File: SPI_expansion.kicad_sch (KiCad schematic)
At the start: 5 parts, among them J1 Conn_02x05_Odd_Even

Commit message: Latest updates
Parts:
- renumbered J1 to J9, R1 to R10, R2 to R11, R3 to R12, R4 to R13
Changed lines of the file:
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@@
 		(dnp no)
 		(fields_autoplaced yes)
-		(property "Reference" "#PWR06"
+		(property "Reference" "#PWR033"
 			(at 172.72 29.21 0)
 			(effects
@@
 			(project ""
 				(path "/38f33acd-ac87-4918-9c1f-d78977d10c9f/f251d033-7c4f-4f74-b0e8-105a8a585980"
-					(reference "#PWR06")
+					(reference "#PWR033")
 					(unit 1)
 				)
@@
 		(dnp no)
 		(fields_autoplaced yes)
-		(property "Reference" "R1"
+		(property "Reference" "R10"
 			(at 168.91 24.13 90)
 			(effects
@@
 			(project ""
 				(path "/38f33acd-ac87-4918-9c1f-d78977d10c9f/f251d033-7c4f-4f74-b0e8-105a8a585980"
-					(reference "R1")
+					(reference "R10")
 					(unit 1)
 				)
@@
 		(dnp no)
 		(fields_autoplaced yes)
-		(property "Reference" "R2"
+		(property "Reference" "R11"
 			(at 168.91 26.67 90)
 			(effects
@@
 			(project "OhWare"
 				(path "/38f33acd-ac87-4918-9c1f-d78977d10c9f/f251d033-7c4f-4f74-b0e8-105a8a585980"
-					(reference "R2")
+					(reference "R11")
 					(unit 1)
 				)
@@
 		(dnp no)
 		(fields_autoplaced yes)
-		(property "Reference" "J1"
+		(property "Reference" "J9"
 			(at 182.88 21.59 0)
 			(effects
@@
 			(project ""
 				(path "/38f33acd-ac87-4918-9c1f-d78977d10c9f/f251d033-7c4f-4f74-b0e8-105a8a585980"
-					(reference "J1")
+					(reference "J9")
 					(unit 1)
 				)
@@
 		(on_board yes)
 		(dnp no)
-		(property "Reference" "R4"
+		(property "Reference" "R13"
 			(at 168.91 31.75 90)
 			(effects
@@
 			(project "OhWare"
 				(path "/38f33acd-ac87-4918-9c1f-d78977d10c9f/f251d033-7c4f-4f74-b0e8-105a8a585980"
-					(reference "R4")
+					(reference "R13")
 					(unit 1)
 				)
@@
 		(dnp no)
 		(fields_autoplaced yes)
-		(property "Reference" "R3"
+		(property "Reference" "R12"
 			(at 168.91 29.21 90)
 			(effects
@@
 			(project "OhWare"
 				(path "/38f33acd-ac87-4918-9c1f-d78977d10c9f/f251d033-7c4f-4f74-b0e8-105a8a585980"
-					(reference "R3")
+					(reference "R12")
 					(unit 1)
 				)
@@
 		(dnp no)
 		(fields_autoplaced yes)
-		(property "Reference" "#PWR05"
+		(property "Reference" "#PWR034"
 			(at 189.23 50.8 0)
 			(effects
@@
 			(project ""
 				(path "/38f33acd-ac87-4918-9c1f-d78977d10c9f/f251d033-7c4f-4f74-b0e8-105a8a585980"
-					(reference "#PWR05")
-					(unit 1)
-				)
+					(reference "#PWR034")
+					(unit 1)
+				)

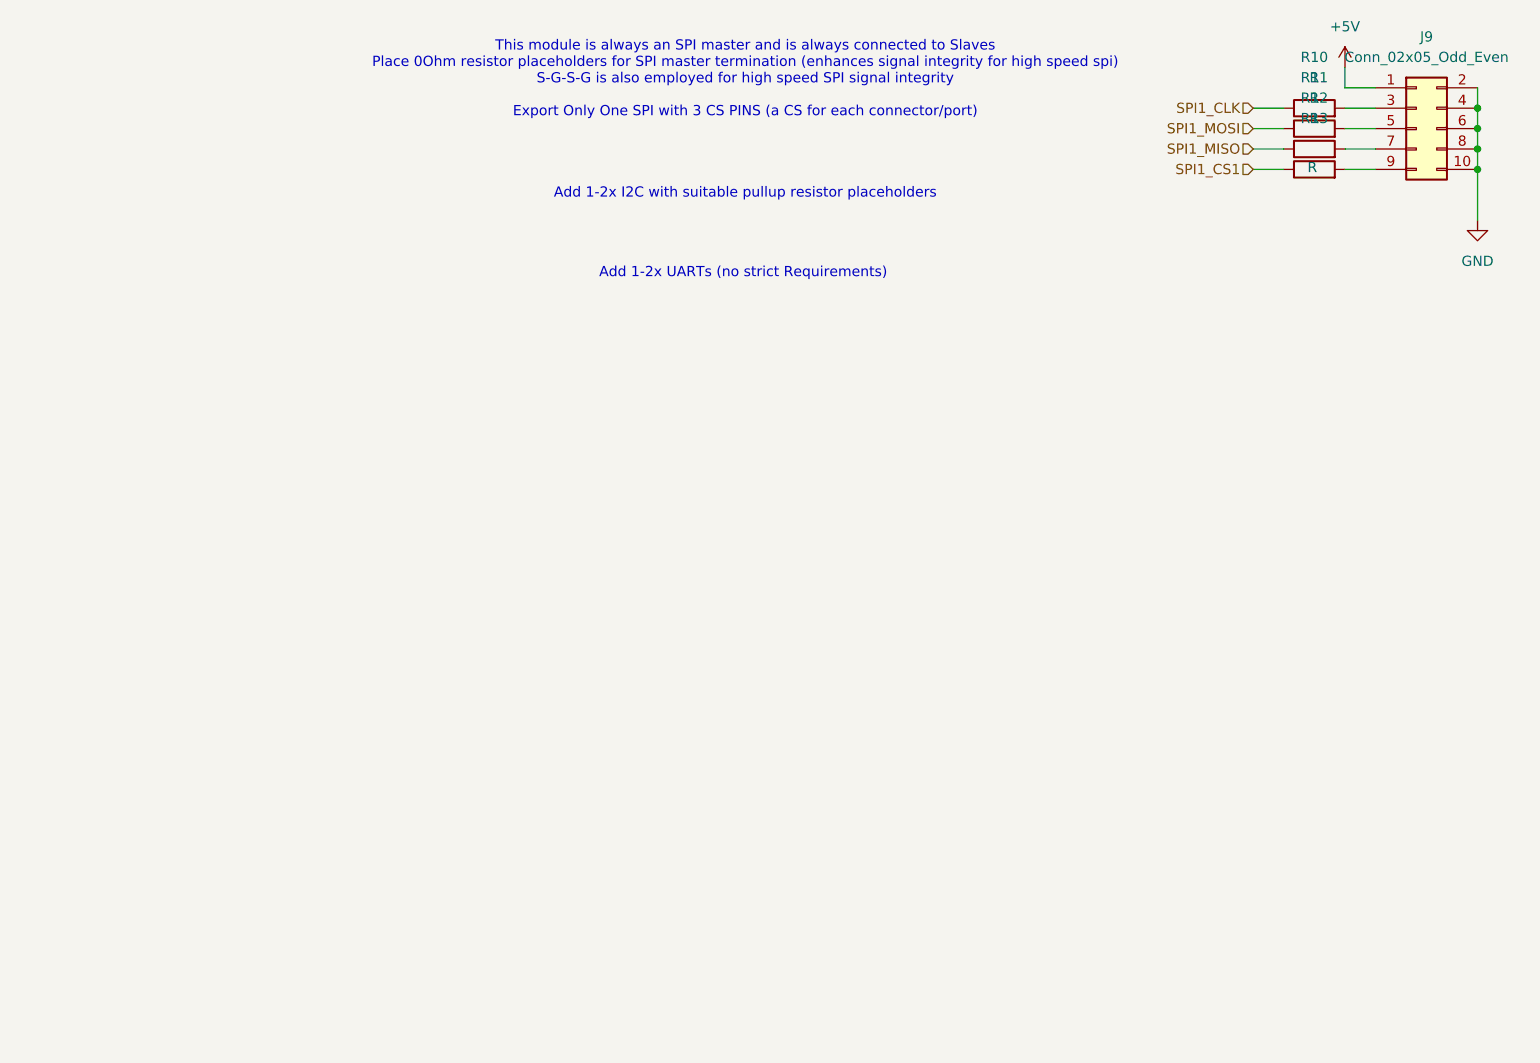
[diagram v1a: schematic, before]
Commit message: added Ethernet and SPI interface
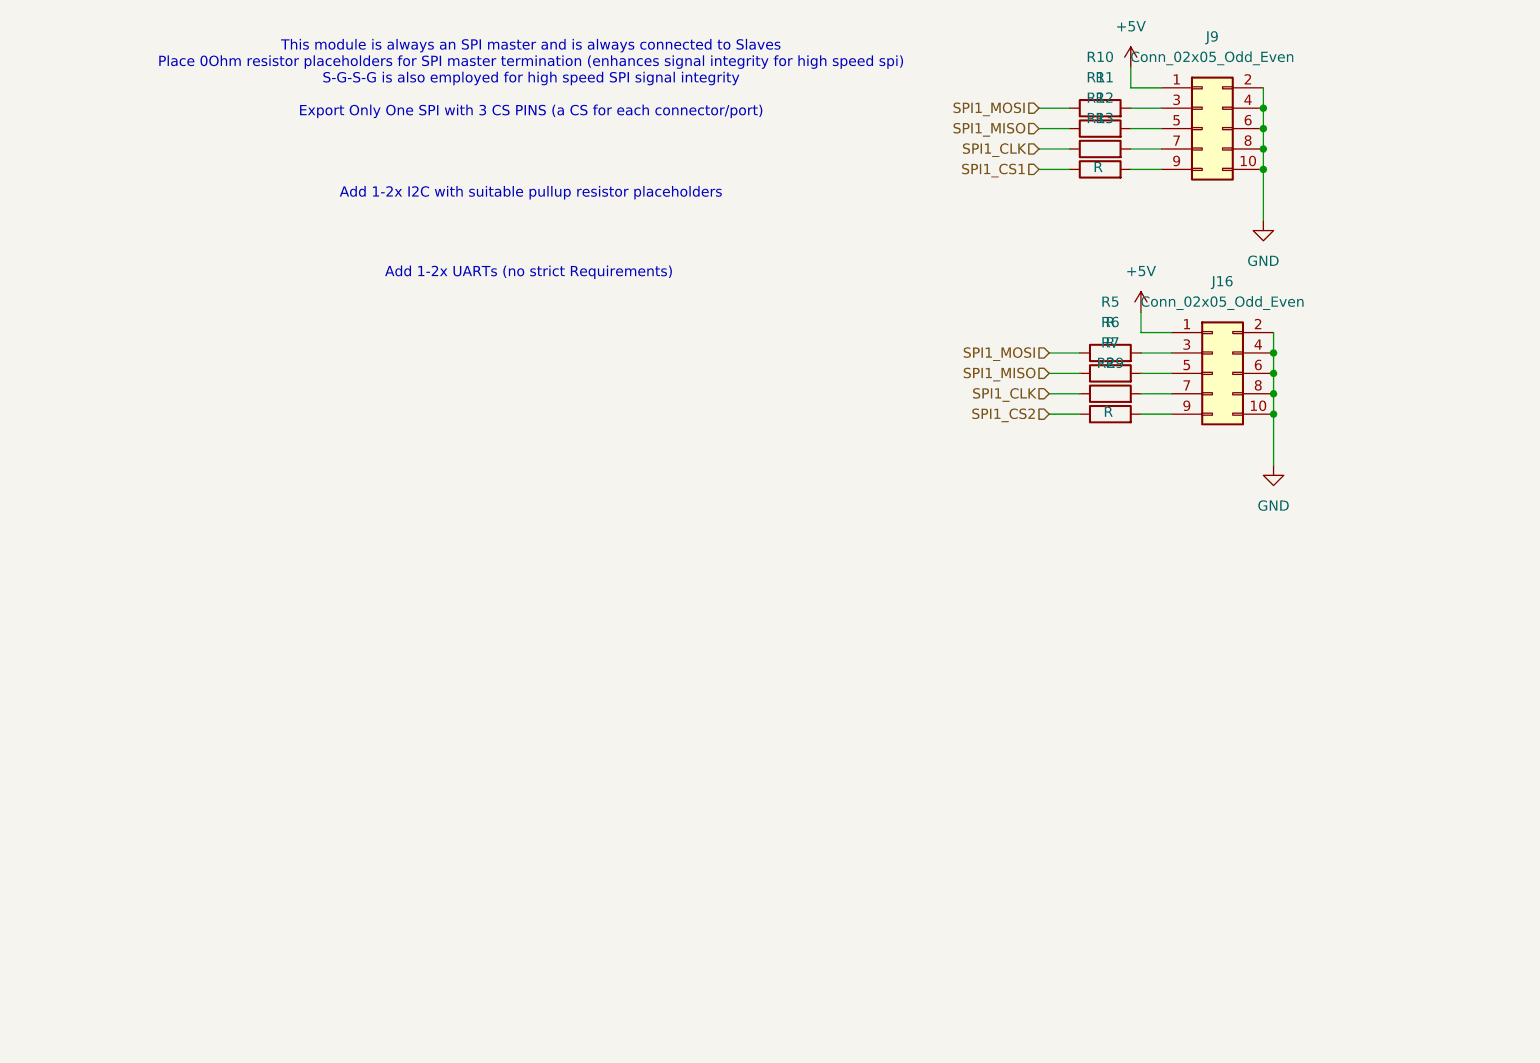
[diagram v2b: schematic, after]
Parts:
- added J16: Conn_02x05_Odd_Even, symbol Connector_Generic:Conn_02x05_Odd_Even
- added R29, R5, R6, R7: R, symbol Device:R
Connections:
- net +5V: now also J16.1 (Pin_1)
- net GND: now also J16.10 (Pin_10), J16.2 (Pin_2), J16.4 (Pin_4), J16.6 (Pin_6), J16.8 (Pin_8)
- net SPI1_CLK: now also R12.1, R7.1; no longer R10.1
- net SPI1_MISO: now also R11.1, R6.1; no longer R12.1
- net SPI1_MOSI: now also R10.1, R5.1; no longer R11.1
- new net: J16.5 (Pin_5), R6.2
- new net: J16.7 (Pin_7), R7.2
- new net: J16.3 (Pin_3), R5.2
- new net: J16.9 (Pin_9), R29.2
- new net SPI1_CS2: R29.1
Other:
- moved on the sheet: J9, R10, R11, R12, R13

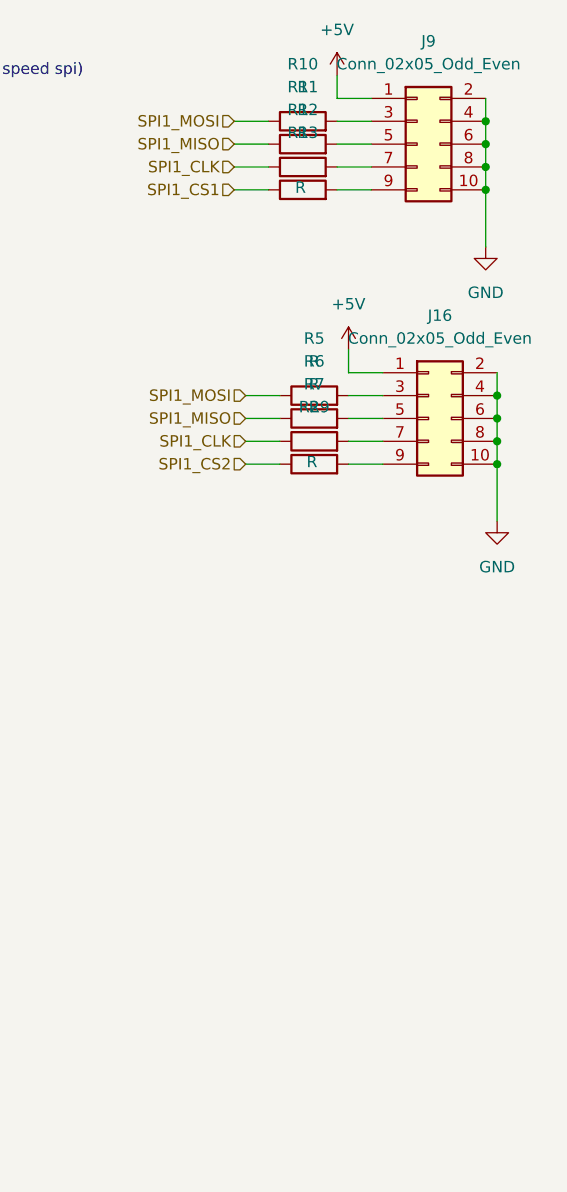
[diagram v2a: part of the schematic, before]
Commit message: Schematic--Footprint link
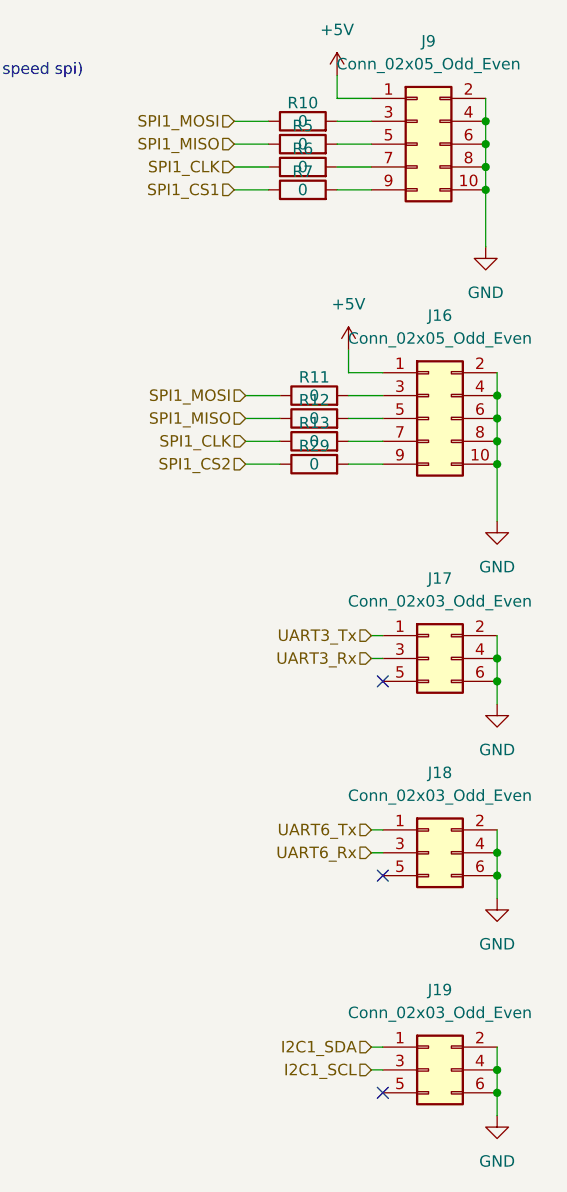
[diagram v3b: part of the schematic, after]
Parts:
- added J17, J18, J19: Conn_02x03_Odd_Even, Connector_IDC:IDC-Header_2x03_P2.54mm_Vertical, symbol Connector_Generic:Conn_02x03_Odd_Even
- J16, J9: footprint (none) -> Connector_IDC:IDC-Header_2x05_P2.54mm_Vertical
- R10, R11, R12, R13, R29, R5, R6, R7: value R -> 0; footprint (none) -> Resistor_SMD:R_0805_2012Metric
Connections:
- net GND: now also J17.2 (Pin_2), J17.4 (Pin_4), J17.6 (Pin_6), J18.2 (Pin_2), J18.4 (Pin_4), J18.6 (Pin_6), J19.2 (Pin_2), J19.4 (Pin_4), J19.6 (Pin_6)
- net SPI1_CLK: now also R13.1, R6.1; no longer R12.1, R7.1
- net SPI1_CS1: now also R7.1; no longer R13.1
- net SPI1_MISO: now also R12.1, R5.1; no longer R11.1, R6.1
- net SPI1_MOSI: now also R11.1; no longer R5.1
- net at R11.2: now also J16.3 (Pin_3); no longer J9.5 (Pin_5)
- net at R6.2: now also J9.7 (Pin_7); no longer J16.5 (Pin_5)
- net at J16.7 (Pin_7): now also R13.2; no longer R7.2
- net at R5.2: now also J9.5 (Pin_5); no longer J16.3 (Pin_3)
- net at R12.2: now also J16.5 (Pin_5); no longer J9.7 (Pin_7)
- net at J9.9 (Pin_9): now also R7.2; no longer R13.2
- new net I2C1_SCL: J19.3 (Pin_3)
- new net I2C1_SDA: J19.1 (Pin_1)
- new net UART3_Rx: J17.3 (Pin_3)
- new net UART3_Tx: J17.1 (Pin_1)
- new net UART6_Rx: J18.3 (Pin_3)
- new net UART6_Tx: J18.1 (Pin_1)
- no-connect marks 0 -> 3
